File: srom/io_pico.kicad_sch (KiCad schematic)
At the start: 7 parts, among them J201 Conn_01x03_Female, J202 Conn_01x06_Female, U201 Pico-2 IO, U202 APS6404L-3SQR_PSRAM64Mbit

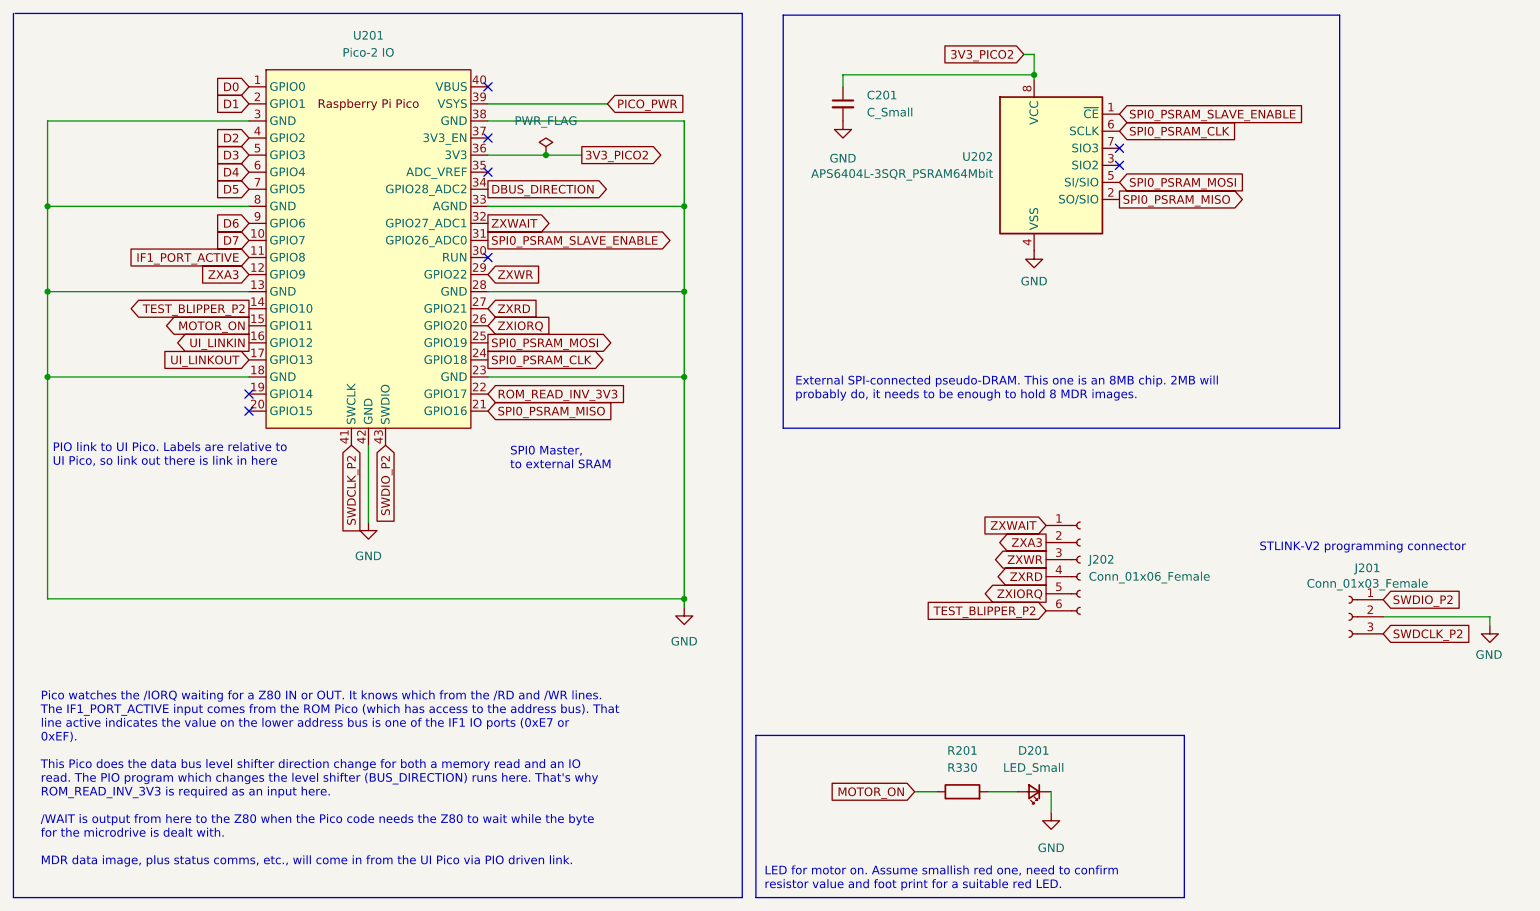
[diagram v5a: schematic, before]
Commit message: add rear edge schematic, RUN switch, ROMCS2 signal
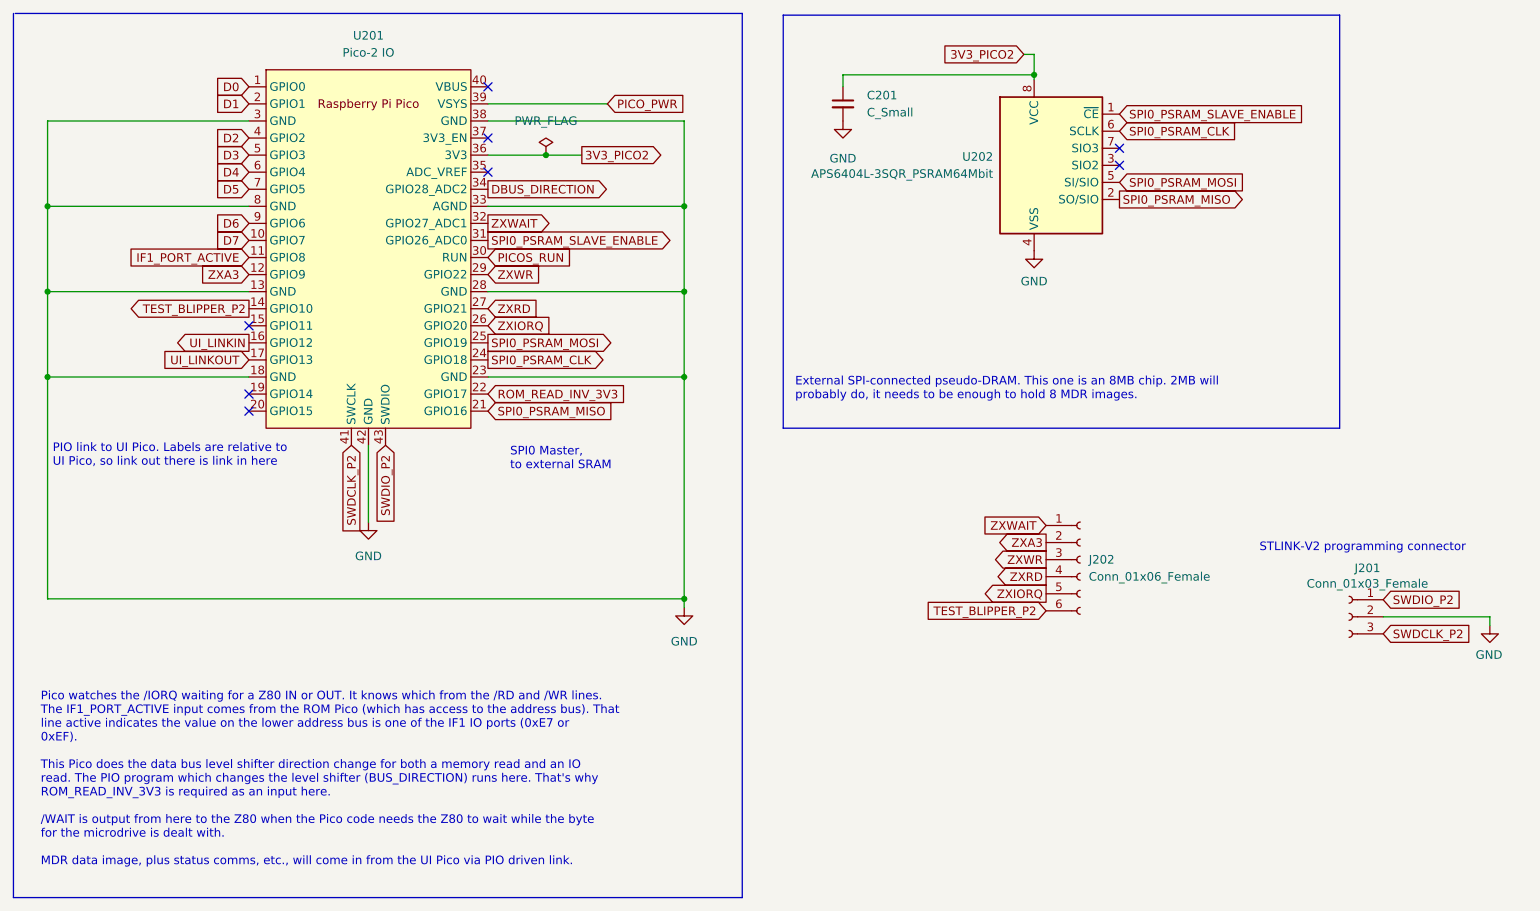
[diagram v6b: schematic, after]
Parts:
- removed D201: LED_Small, LED_THT:LED_D3.0mm, symbol Device:LED_Small
- removed R201: R330, Resistor_SMD:R_1206_3216Metric_Pad1.30x1.75mm_HandSolder, symbol Device:R
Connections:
- net PICOS_RUN: now reaches U201.30 (RUN)
- net MOTOR_ON: no longer names the net of U201.15 (GPIO11)
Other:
- note removed: "LED for motor on. Assume smallish red one, need to confirm resistor value and foot print for a suitable red LED."
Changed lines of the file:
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@@
   (title_block
     (title "Pico Interface One")
-    (date "2023-04-18")
+    (date "2023-06-16")
     (rev "v1.4WIP")
   )
@@
   (no_connect (at 92.202 38.608))
   (no_connect (at 186.182 40.132))
-  (no_connect (at 92.202 56.388))
+  (no_connect (at 56.642 66.548))
   (no_connect (at 56.642 79.248))
-  (polyline (pts (xy 195.834 127.508) (xy 132.08 127.508))
-    (stroke (width 0) (type default) (color 0 0 0 0))
-  )
-  (wire (pts (xy 166.624 135.89) (xy 170.942 135.89))
-    (stroke (width 0) (type default) (color 0 0 0 0))
-  )
   (wire (pts (xy 26.67 61.468) (xy 56.642 61.468))
     (stroke (width 0) (type default) (color 0 0 0 0))
@@
     (stroke (width 0) (type default) (color 0 0 0 0))
   )
-  (wire (pts (xy 176.022 138.938) (xy 176.022 135.89))
-    (stroke (width 0) (type default) (color 0 0 0 0))
-  )
   (polyline (pts (xy 218.948 20.32) (xy 218.948 81.788))
     (stroke (width 0) (type default) (color 0 0 0 0))
@@
     (stroke (width 0) (type default) (color 0 0 0 0))
   )
-  (polyline (pts (xy 195.834 151.638) (xy 195.834 127.508))
-    (stroke (width 0) (type default) (color 0 0 0 0))
-  )
   (wire (pts (xy 74.422 84.328) (xy 74.422 95.758))
     (stroke (width 0) (type default) (color 0 0 0 0))
@@
     (stroke (width 0) (type default) (color 0 0 0 0))
   )
-  (polyline (pts (xy 132.08 151.638) (xy 195.834 151.638))
-    (stroke (width 0) (type default) (color 0 0 0 0))
-  )
   (wire (pts (xy 26.67 74.168) (xy 26.67 107.188))
     (stroke (width 0) (type default) (color 0 0 0 0))
@@
     (stroke (width 0) (type default) (color 0 0 0 0))
   )
-  (polyline (pts (xy 132.08 127.508) (xy 132.08 151.638))
-    (stroke (width 0) (type default) (color 0 0 0 0))
-  )
   (wire (pts (xy 100.838 41.148) (xy 106.172 41.148))
-    (stroke (width 0) (type default) (color 0 0 0 0))
-  )
-  (wire (pts (xy 155.702 135.89) (xy 159.004 135.89))
     (stroke (width 0) (type default) (color 0 0 0 0))
   )
@@
     (effects (font (size 1.27 1.27)) (justify left bottom))
   )
-  (text "LED for motor on. Assume smallish red one, need to confirm\nresistor value and foot print for a suitable red LED."
-    (at 133.35 150.622 0)
-    (effects (font (size 1.27 1.27)) (justify left bottom))
-  )
   (global_label "ZXIORQ" (shape output) (at 175.26 106.426 180) (fields_autoplaced)
     (effects (font (size 1.27 1.27)) (justify right))
@@
     )
   )
-  (global_label "MOTOR_ON" (shape output) (at 56.642 66.548 180) (fields_autoplaced)
-    (effects (font (size 1.27 1.27)) (justify right))
-    (property "Intersheet References" "${INTERSHEET_REFS}" (id 0) (at 44.2503 66.4686 0)
-      (effects (font (size 1.27 1.27)) (justify right) hide)
-    )
-  )
   (global_label "3V3_PICO2" (shape input) (at 171.958 26.162 180) (fields_autoplaced)
     (effects (font (size 1.27 1.27)) (justify right))
@@
     )
   )
+  (global_label "PICOS_RUN" (shape input) (at 92.202 56.388 0) (fields_autoplaced)
+    (effects (font (size 1.27 1.27)) (justify left))
+    (property "Intersheet References" "${INTERSHEET_REFS}" (id 0) (at 105.1984 56.3086 0)
+      (effects (font (size 1.27 1.27)) (justify left) hide)
+    )
+  )
   (global_label "SPI0_PSRAM_CLK" (shape input) (at 186.182 37.592 0) (fields_autoplaced)
     (effects (font (size 1.27 1.27)) (justify left))
@@
     )
   )
-  (global_label "MOTOR_ON" (shape input) (at 155.702 135.89 180) (fields_autoplaced)
-    (effects (font (size 1.27 1.27)) (justify right))
-    (property "Intersheet References" "${INTERSHEET_REFS}" (id 0) (at 143.3103 135.8106 0)
-      (effects (font (size 1.27 1.27)) (justify right) hide)
-    )
-  )
   (global_label "ZXRD" (shape input) (at 92.202 64.008 0) (fields_autoplaced)
     (effects (font (size 1.27 1.27)) (justify left))
@@
       (effects (font (size 1.27 1.27)) (justify right) hide)
     )
-  )
-  (symbol (lib_id "power:GND") (at 176.022 138.938 0) (unit 1)
-    (in_bom yes) (on_board yes) (fields_autoplaced)
-    (property "Reference" "#PWR0106" (id 0) (at 176.022 145.288 0)
-      (effects (font (size 1.27 1.27)) hide)
-    )
-    (property "Value" "GND" (id 1) (at 176.022 144.272 0))
-    (property "Footprint" "" (id 2) (at 176.022 138.938 0)
-      (effects (font (size 1.27 1.27)) hide)
-    )
-    (property "Datasheet" "" (id 3) (at 176.022 138.938 0)
-      (effects (font (size 1.27 1.27)) hide)
-    )
-    (pin "1")
   )
   (symbol (lib_id "power:PWR_FLAG") (at 100.838 41.148 0) (unit 1)
@@
     )
     (pin "1")
-  )
-  (symbol (lib_id "Device:LED_Small") (at 173.482 135.89 180) (unit 1)
-    (in_bom yes) (on_board yes) (fields_autoplaced)
-    (property "Reference" "D201" (id 0) (at 173.4185 129.794 0))
-    (property "Value" "LED_Small" (id 1) (at 173.4185 132.334 0))
-    (property "Footprint" "LED_THT:LED_D3.0mm" (id 2) (at 173.482 135.89 90)
-      (effects (font (size 1.27 1.27)) hide)
-    )
-    (property "Datasheet" "~" (id 3) (at 173.482 135.89 90)
-      (effects (font (size 1.27 1.27)) hide)
-    )
-    (pin "1")
-    (pin "2")
   )
   (symbol (lib_id "Connector:Conn_01x03_Female") (at 220.345 109.855 0) (mirror y) (unit 1)
@@
     (pin "1")
   )
-  (symbol (lib_id "Device:R") (at 162.814 135.89 90) (unit 1)
-    (in_bom yes) (on_board yes) (fields_autoplaced)
-    (property "Reference" "R201" (id 0) (at 162.814 129.794 90))
-    (property "Value" "R330" (id 1) (at 162.814 132.334 90))
-    (property "Footprint" "Resistor_SMD:R_1206_3216Metric_Pad1.30x1.75mm_HandSolder" (id 2) (at 162.814 137.668 90)
-      (effects (font (size 1.27 1.27)) hide)
-    )
-    (property "Datasheet" "~" (id 3) (at 162.814 135.89 0)
-      (effects (font (size 1.27 1.27)) hide)
-    )
-    (pin "1")
-    (pin "2")
-  )
   (symbol (lib_id "Connector:Conn_01x06_Female") (at 180.34 101.346 0) (unit 1)

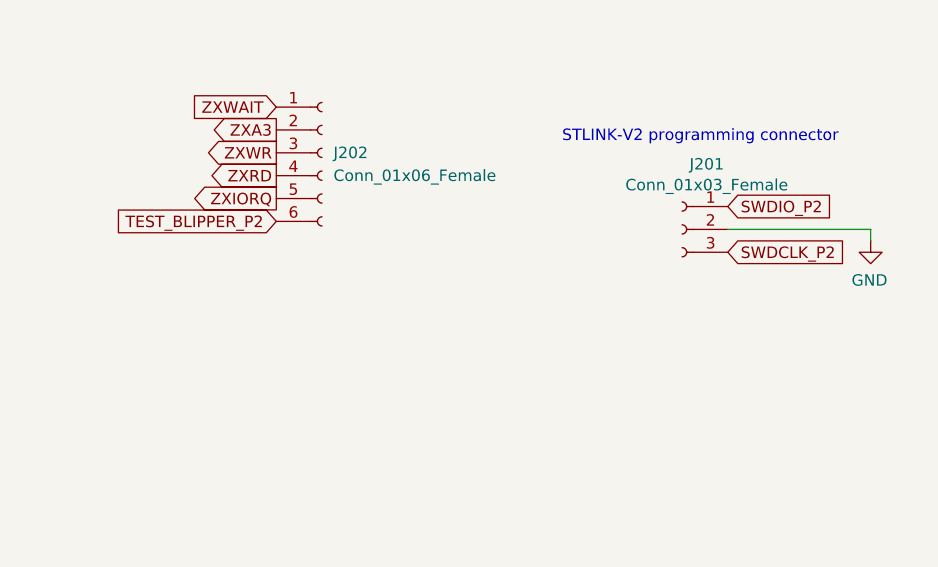
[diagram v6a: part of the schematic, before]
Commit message: remove test point connectors, no needed on next board (famous last words)
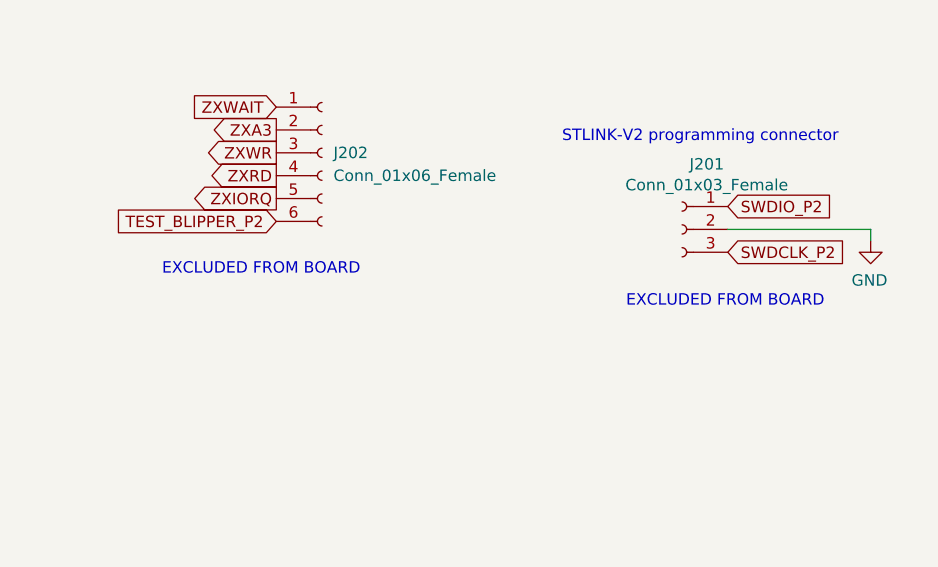
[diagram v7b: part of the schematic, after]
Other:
- note added: "EXCLUDED FROM BOARD"
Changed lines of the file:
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@@
+    (effects (font (size 1.27 1.27)) (justify left bottom))
+  )
+  (text "EXCLUDED FROM BOARD" (at 214.122 118.618 0)
+    (effects (font (size 1.27 1.27)) (justify left bottom))
+  )
+  (text "EXCLUDED FROM BOARD" (at 162.56 115.062 0)
     (effects (font (size 1.27 1.27)) (justify left bottom))
   )
@@
   )
   (symbol (lib_id "Connector:Conn_01x03_Female") (at 220.345 109.855 0) (mirror y) (unit 1)
-    (in_bom yes) (on_board yes)
+    (in_bom yes) (on_board no)
     (property "Reference" "J201" (id 0) (at 223.0882 102.616 0))
     (property "Value" "Conn_01x03_Female" (id 1) (at 223.0882 104.9274 0))
@@
   )
   (symbol (lib_id "Connector:Conn_01x06_Female") (at 180.34 101.346 0) (unit 1)
-    (in_bom yes) (on_board yes) (fields_autoplaced)
+    (in_bom yes) (on_board no) (fields_autoplaced)
     (property "Reference" "J202" (id 0) (at 181.61 101.3459 0)
       (effects (font (size 1.27 1.27)) (justify left))
